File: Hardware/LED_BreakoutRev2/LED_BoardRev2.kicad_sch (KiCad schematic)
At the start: 29 parts

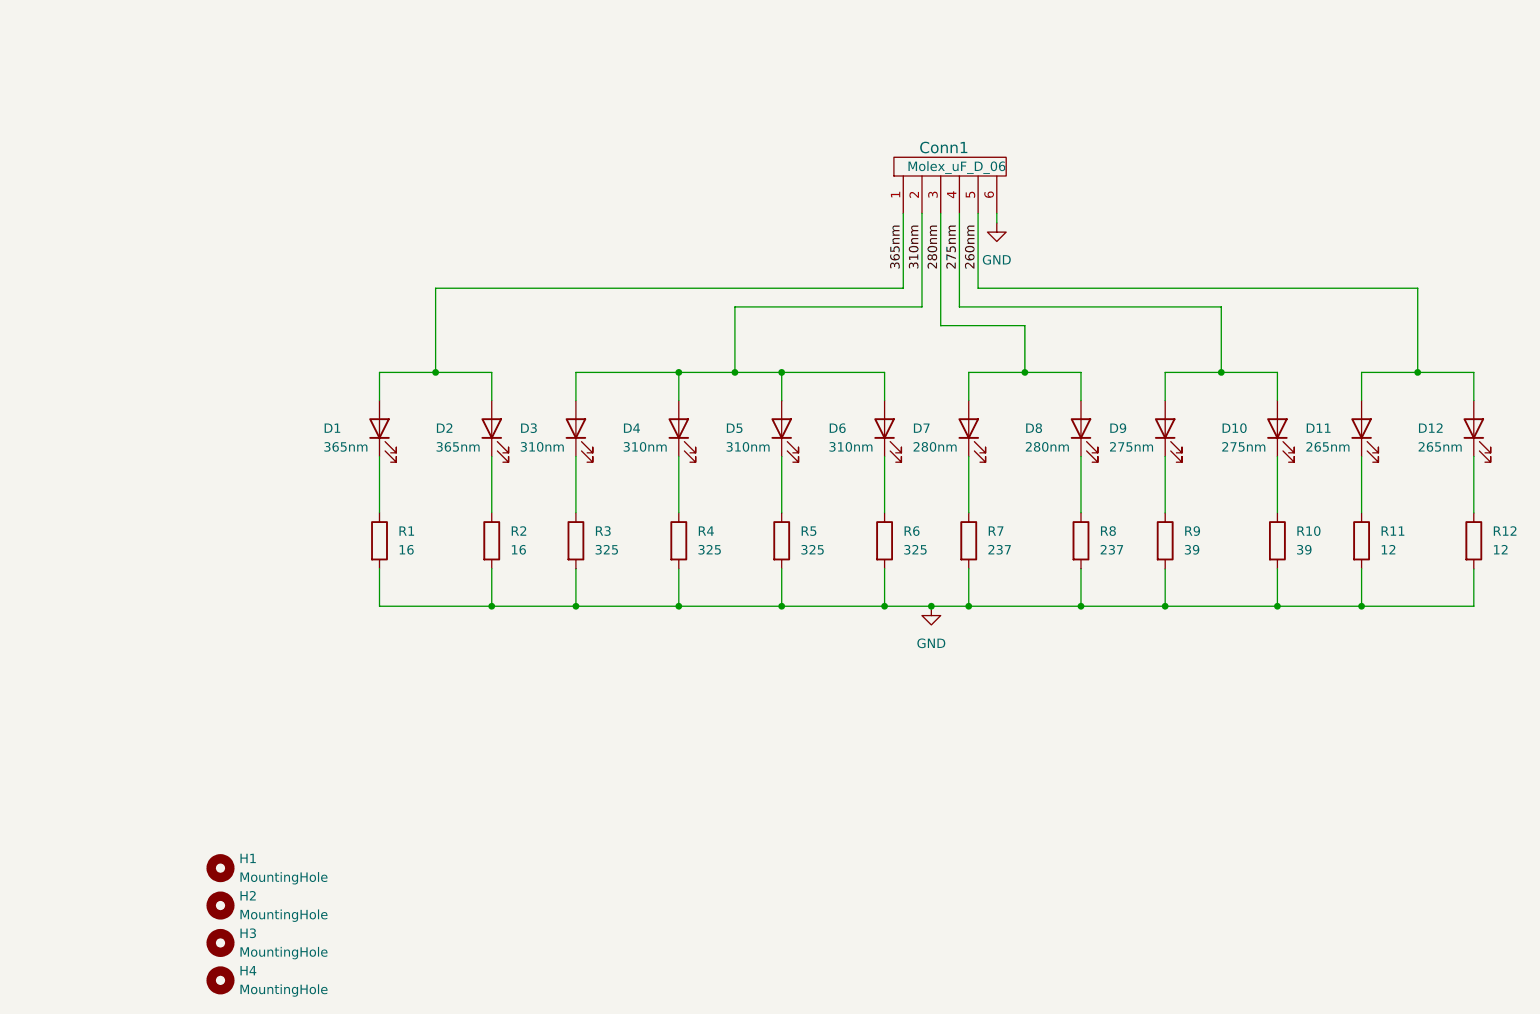
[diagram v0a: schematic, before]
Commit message: page edits for printing
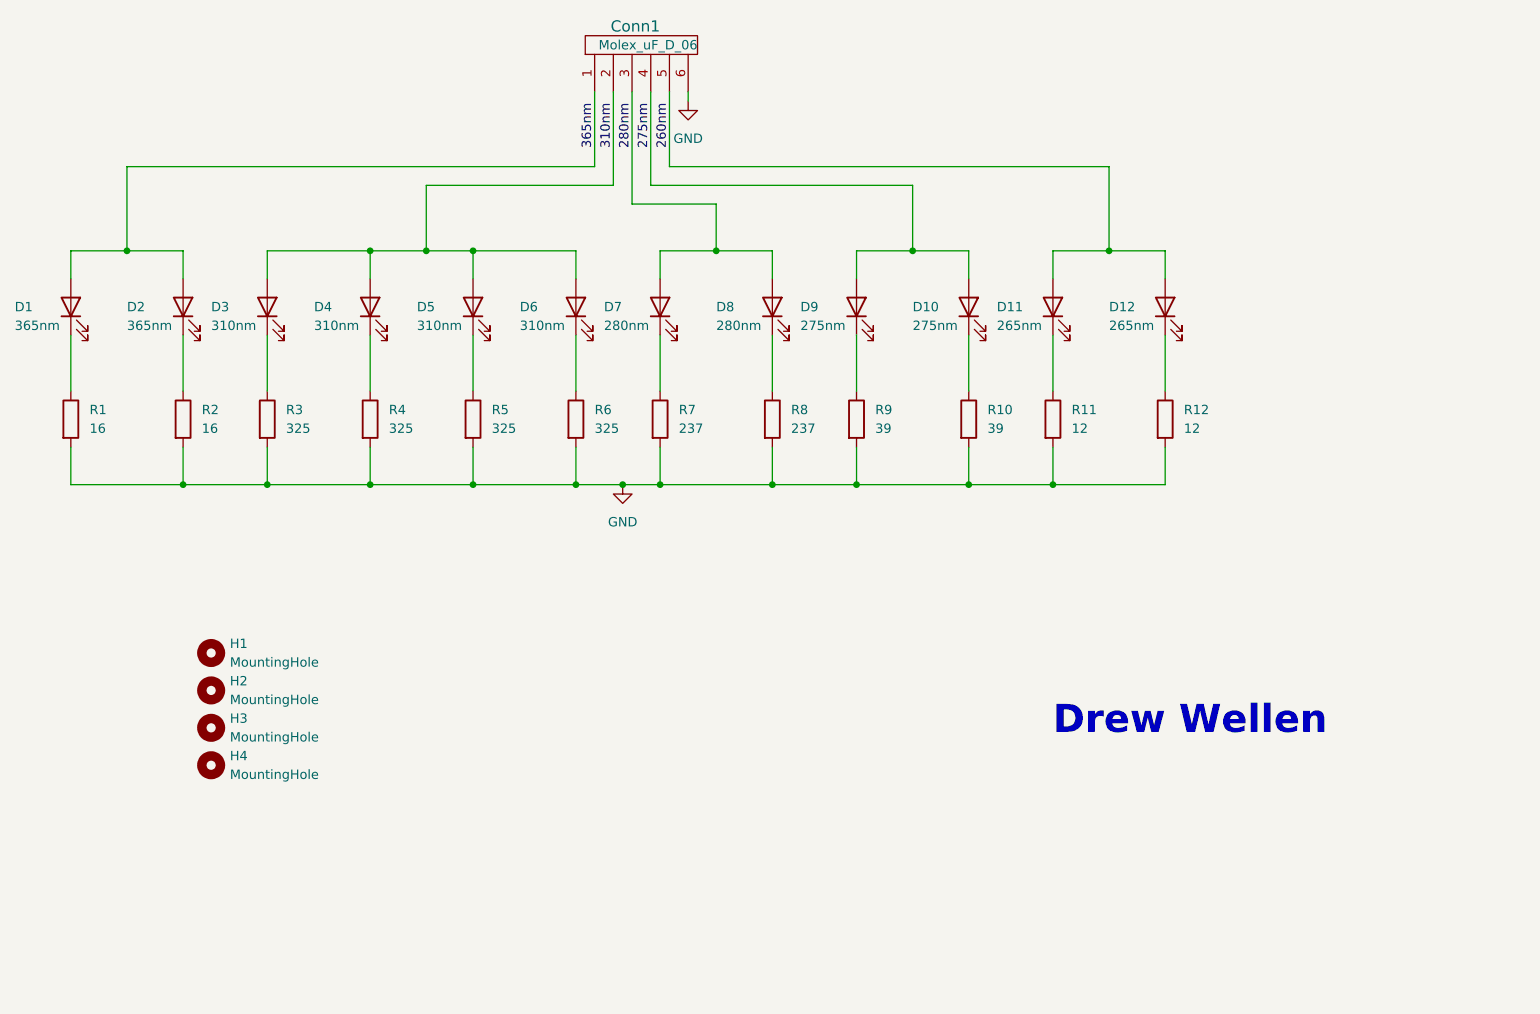
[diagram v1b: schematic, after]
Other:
- note added: "Drew Wellen"
- company: (none) -> Mars Rover Design Team
- title: (none) -> UV LED Board
- moved on the sheet: Conn1, D1, D10, D11, D12, D2, D3, D4, D5, D6, D7, D8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
